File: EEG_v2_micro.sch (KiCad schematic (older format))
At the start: 34 parts, among them SW2 SW_PUSH, SW3 SW_PUSH, U6 CC2540, U7 2450BM15A0002E, X1 32-MHz, X2 32-MHz

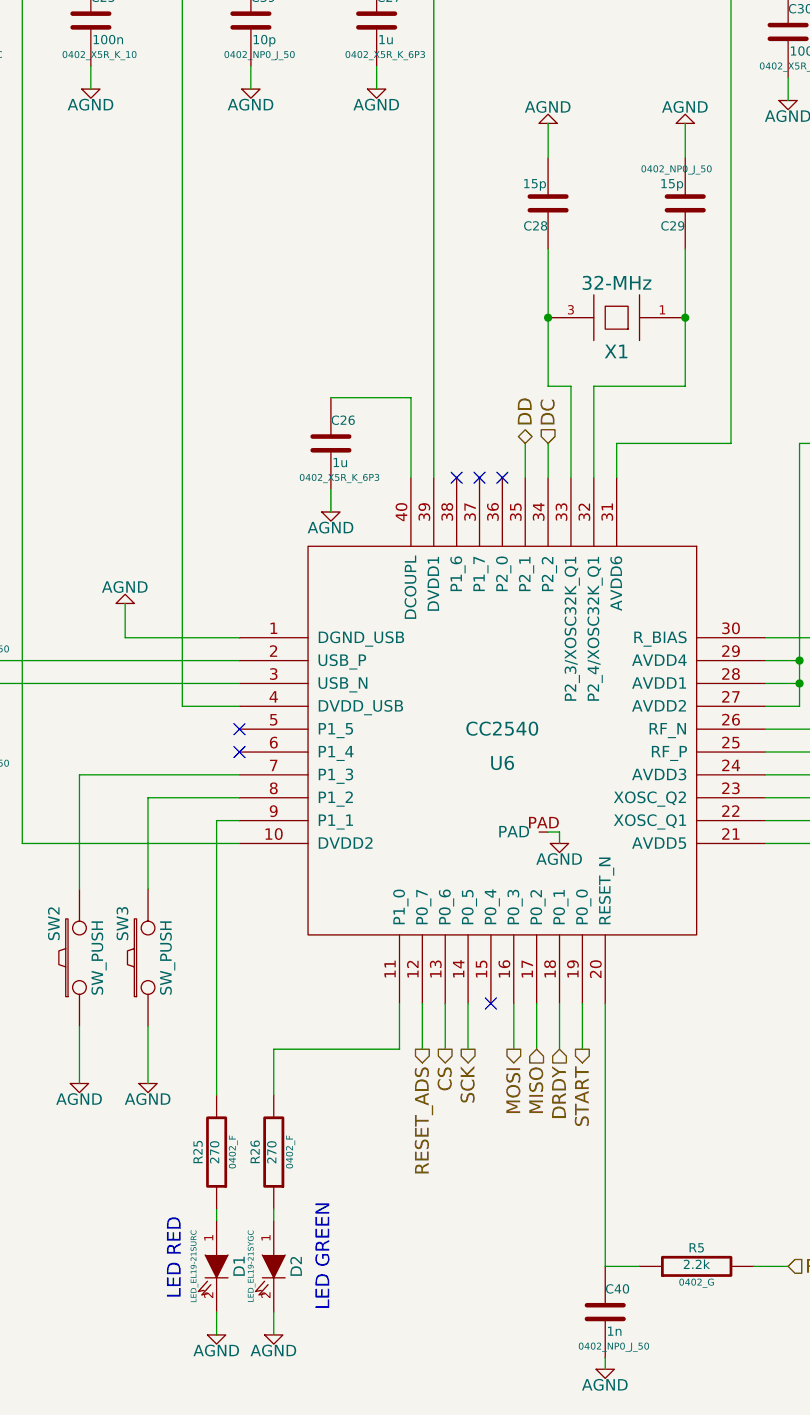
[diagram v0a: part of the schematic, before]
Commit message: Add footprints
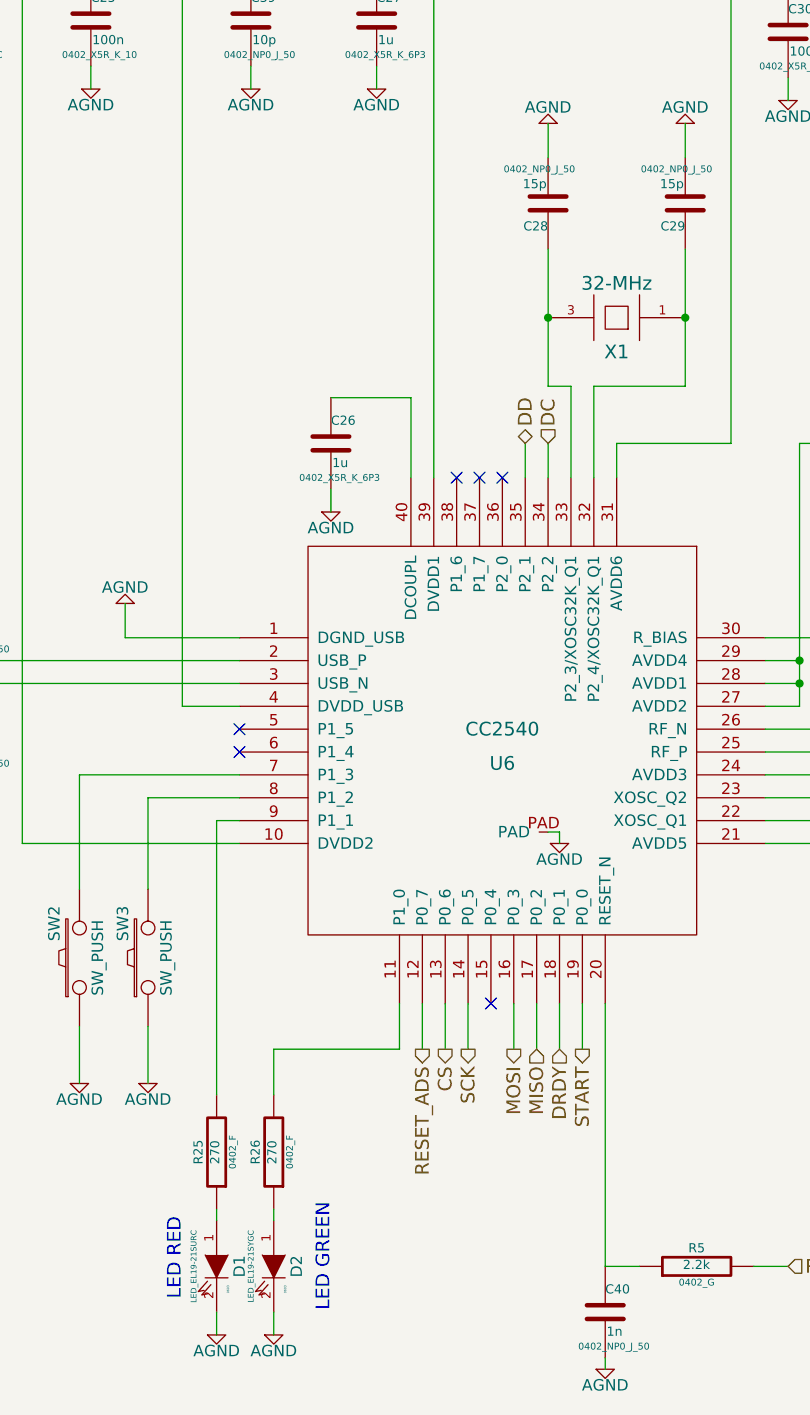
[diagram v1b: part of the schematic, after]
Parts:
- C28: footprint ~ -> 0402_NP0_J_50
- D1, D2: footprint ~ -> 0603
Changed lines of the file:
@@
 $EndComp
 $Comp
-L AGND #PWR038
+L AGND #PWR040
 U 1 1 54B4DC2F
 P 3400 3850
-F 0 "#PWR038" H 3400 3850 40  0001 C CNN
+F 0 "#PWR040" H 3400 3850 40  0001 C CNN
 F 1 "AGND" H 3400 3780 50  0000 C CNN
 F 2 "~" H 3400 3850 60  0000 C CNN
@@
 $EndComp
 $Comp
-L AGND #PWR039
+L AGND #PWR041
 U 1 1 54B4DEBC
 P 6550 4450
-F 0 "#PWR039" H 6550 4450 40  0001 C CNN
+F 0 "#PWR041" H 6550 4450 40  0001 C CNN
 F 1 "AGND" H 6550 4380 50  0000 C CNN
 F 2 "~" H 6550 4450 60  0000 C CNN
@@
 $EndComp
 $Comp
-L +3.3V #PWR040
+L +3.3V #PWR042
 U 1 1 54B4DF64
 P 650 1400
-F 0 "#PWR040" H 650 1360 30  0001 C CNN
+F 0 "#PWR042" H 650 1360 30  0001 C CNN
 F 1 "+3.3V" H 650 1510 30  0000 C CNN
 F 2 "~" H 650 1400 60  0000 C CNN
@@
 $EndComp
 $Comp
-L AGND #PWR041
+L AGND #PWR043
 U 1 1 54B4E155
 P 5750 6600
-F 0 "#PWR041" H 5750 6600 40  0001 C CNN
+F 0 "#PWR043" H 5750 6600 40  0001 C CNN
 F 1 "AGND" H 5750 6530 50  0000 C CNN
 F 2 "~" H 5750 6600 60  0000 C CNN
@@
 $EndComp
 $Comp
-L AGND #PWR042
+L AGND #PWR044
 U 1 1 54B4E15B
 P 6350 6600
-F 0 "#PWR042" H 6350 6600 40  0001 C CNN
+F 0 "#PWR044" H 6350 6600 40  0001 C CNN
 F 1 "AGND" H 6350 6530 50  0000 C CNN
 F 2 "~" H 6350 6600 60  0000 C CNN
@@
 F 0 "C28" H 4350 2600 40  0000 L CNN
 F 1 "15p" H 4356 2415 40  0000 L CNN
-F 2 "~" H 4388 2350 30  0000 C CNN
+F 2 "0402_NP0_J_50" H 4388 2350 30  0000 C CNN
 F 3 "~" H 4350 2500 60  0000 C CNN
 	1    4350 2500
@@
 $EndComp
 $Comp
-L AGND #PWR043
+L AGND #PWR045
 U 1 1 54B4E36D
 P 4950 2150
-F 0 "#PWR043" H 4950 2150 40  0001 C CNN
+F 0 "#PWR045" H 4950 2150 40  0001 C CNN
 F 1 "AGND" H 4950 2080 50  0000 C CNN
 F 2 "~" H 4950 2150 60  0000 C CNN
@@
 $EndComp
 $Comp
-L AGND #PWR044
+L AGND #PWR046
 U 1 1 54B4E373
 P 4350 2150
-F 0 "#PWR044" H 4350 2150 40  0001 C CNN
+F 0 "#PWR046" H 4350 2150 40  0001 C CNN
 F 1 "AGND" H 4350 2080 50  0000 C CNN
 F 2 "~" H 4350 2150 60  0000 C CNN
@@
 $EndComp
 $Comp
-L AGND #PWR045
+L AGND #PWR047
 U 1 1 54B4E516
 P 4400 5300
-F 0 "#PWR045" H 4400 5300 40  0001 C CNN
+F 0 "#PWR047" H 4400 5300 40  0001 C CNN
 F 1 "AGND" H 4400 5230 50  0000 C CNN
 F 2 "~" H 4400 5300 60  0000 C CNN
@@
 $EndComp
 $Comp
-L AGND #PWR046
+L AGND #PWR048
 U 1 1 54B4E69D
 P 2500 4250
-F 0 "#PWR046" H 2500 4250 40  0001 C CNN
+F 0 "#PWR048" H 2500 4250 40  0001 C CNN
 F 1 "AGND" H 2500 4180 50  0000 C CNN
 F 2 "~" H 2500 4250 60  0000 C CNN
@@
 $EndComp
 $Comp
-L AGND #PWR047
+L AGND #PWR049
 U 1 1 54B6FF14
 P 2350 2000
-F 0 "#PWR047" H 2350 2000 40  0001 C CNN
+F 0 "#PWR049" H 2350 2000 40  0001 C CNN
 F 1 "AGND" H 2350 1930 50  0000 C CNN
 F 2 "~" H 2350 2000 60  0000 C CNN
@@
 $EndComp
 $Comp
-L AGND #PWR048
+L AGND #PWR050
 U 1 1 54B7020B
 P 1700 2000
-F 0 "#PWR048" H 1700 2000 40  0001 C CNN
+F 0 "#PWR050" H 1700 2000 40  0001 C CNN
 F 1 "AGND" H 1700 1930 50  0000 C CNN
 F 2 "~" H 1700 2000 60  0000 C CNN
@@
 $EndComp
 $Comp
-L AGND #PWR049
+L AGND #PWR051
 U 1 1 54B703A3
 P 3600 2000
-F 0 "#PWR049" H 3600 2000 40  0001 C CNN
+F 0 "#PWR051" H 3600 2000 40  0001 C CNN
 F 1 "AGND" H 3600 1930 50  0000 C CNN
 F 2 "~" H 3600 2000 60  0000 C CNN
@@
 $EndComp
 $Comp
-L AGND #PWR050
+L AGND #PWR052
 U 1 1 54B708CD
 P 5400 2050
-F 0 "#PWR050" H 5400 2050 40  0001 C CNN
+F 0 "#PWR052" H 5400 2050 40  0001 C CNN
 F 1 "AGND" H 5400 1980 50  0000 C CNN
 F 2 "~" H 5400 2050 60  0000 C CNN
@@
 $EndComp
 $Comp
-L AGND #PWR051
+L AGND #PWR053
 U 1 1 54B70B07
 P 5950 2050
-F 0 "#PWR051" H 5950 2050 40  0001 C CNN
+F 0 "#PWR053" H 5950 2050 40  0001 C CNN
 F 1 "AGND" H 5950 1980 50  0000 C CNN
 F 2 "~" H 5950 2050 60  0000 C CNN
@@
 $EndComp
 $Comp
-L AGND #PWR052
+L AGND #PWR054
 U 1 1 54B70B14
 P 6350 2050
-F 0 "#PWR052" H 6350 2050 40  0001 C CNN
+F 0 "#PWR054" H 6350 2050 40  0001 C CNN
 F 1 "AGND" H 6350 1980 50  0000 C CNN
 F 2 "~" H 6350 2050 60  0000 C CNN
@@
 $EndComp
 $Comp
-L AGND #PWR053
+L AGND #PWR055
 U 1 1 54B71005
 P 6950 2050
-F 0 "#PWR053" H 6950 2050 40  0001 C CNN
+F 0 "#PWR055" H 6950 2050 40  0001 C CNN
 F 1 "AGND" H 6950 1980 50  0000 C CNN
 F 2 "~" H 6950 2050 60  0000 C CNN
@@
 $EndComp
 $Comp
-L AGND #PWR054
+L AGND #PWR056
 U 1 1 54B71061
 P 7500 2050
-F 0 "#PWR054" H 7500 2050 40  0001 C CNN
+F 0 "#PWR056" H 7500 2050 40  0001 C CNN
 F 1 "AGND" H 7500 1980 50  0000 C CNN
 F 2 "~" H 7500 2050 60  0000 C CNN
@@
 $EndComp
 $Comp
-L AGND #PWR055
+L AGND #PWR057
 U 1 1 54B71D5A
 P 8450 5400
-F 0 "#PWR055" H 8450 5400 40  0001 C CNN
+F 0 "#PWR057" H 8450 5400 40  0001 C CNN
 F 1 "AGND" H 8450 5330 50  0000 C CNN
 F 2 "~" H 8450 5400 60  0000 C CNN
@@
 $EndComp
 $Comp
-L AGND #PWR056
+L AGND #PWR058
 U 1 1 54B75306
 P 3050 2000
-F 0 "#PWR056" H 3050 2000 40  0001 C CNN
+F 0 "#PWR058" H 3050 2000 40  0001 C CNN
 F 1 "AGND" H 3050 1930 50  0000 C CNN
 F 2 "~" H 3050 2000 60  0000 C CNN
@@
 $EndComp
 $Comp
-L AGND #PWR057
+L AGND #PWR059
 U 1 1 54B75999
 P 1800 5050
-F 0 "#PWR057" H 1800 5050 40  0001 C CNN
+F 0 "#PWR059" H 1800 5050 40  0001 C CNN
 F 1 "AGND" H 1800 4980 50  0000 C CNN
 F 2 "~" H 1800 5050 60  0000 C CNN
@@
 $EndComp
 $Comp
-L AGND #PWR058
+L AGND #PWR060
 U 1 1 54B7599F
 P 1800 4000
-F 0 "#PWR058" H 1800 4000 40  0001 C CNN
+F 0 "#PWR060" H 1800 4000 40  0001 C CNN
 F 1 "AGND" H 1800 3930 50  0000 C CNN
 F 2 "~" H 1800 4000 60  0000 C CNN
@@
 	4600 6000 4600 7150
 $Comp
-L AGND #PWR059
+L AGND #PWR061
 U 1 1 54C2E9F6
 P 4600 7600
-F 0 "#PWR059" H 4600 7600 40  0001 C CNN
+F 0 "#PWR061" H 4600 7600 40  0001 C CNN
 F 1 "AGND" H 4600 7530 50  0000 C CNN
 F 2 "~" H 4600 7600 60  0000 C CNN
@@
 $EndComp
 $Comp
-L AGND #PWR060
+L AGND #PWR062
 U 1 1 54C2ED03
 P 9900 5550
-F 0 "#PWR060" H 9900 5550 40  0001 C CNN
+F 0 "#PWR062" H 9900 5550 40  0001 C CNN
 F 1 "AGND" H 9900 5480 50  0000 C CNN
 F 2 "~" H 9900 5550 60  0000 C CNN
@@
 $EndComp
 $Comp
-L AGND #PWR061
+L AGND #PWR063
 U 1 1 54C2EF06
 P 9450 4200
-F 0 "#PWR061" H 9450 4200 40  0001 C CNN
+F 0 "#PWR063" H 9450 4200 40  0001 C CNN
 F 1 "AGND" H 9450 4130 50  0000 C CNN
 F 2 "~" H 9450 4200 60  0000 C CNN
@@
 	2300 6100 2300 6350
 $Comp
-L AGND #PWR062
+L AGND #PWR064
 U 1 1 54CBF6E0
 P 2300 6350
-F 0 "#PWR062" H 2300 6350 40  0001 C CNN
+F 0 "#PWR064" H 2300 6350 40  0001 C CNN
 F 1 "AGND" H 2300 6280 50  0000 C CNN
 F 2 "~" H 2300 6350 60  0000 C CNN
@@
 	2600 6100 2600 6350
 $Comp
-L AGND #PWR063
+L AGND #PWR065
 U 1 1 54CBFC8B
 P 2600 6350
-F 0 "#PWR063" H 2600 6350 40  0001 C CNN
+F 0 "#PWR065" H 2600 6350 40  0001 C CNN
 F 1 "AGND" H 2600 6280 50  0000 C CNN
 F 2 "~" H 2600 6350 60  0000 C CNN
@@
 F 0 "D1" H 2900 7250 50  0000 C CNN
 F 1 "LED_EL19-21SURC" H 2900 7050 25  0000 C CNN
-F 2 "~" H 2900 7150 60  0000 C CNN
+F 2 "0603" H 3000 7200 10  0000 C CNN
 F 3 "~" H 2900 7150 60  0000 C CNN
 	1    2900 7150
@@
 F 0 "D2" H 3150 7250 50  0000 C CNN
 F 1 "LED_EL19-21SYGC" H 3150 7050 25  0000 C CNN
-F 2 "~" H 3150 7150 60  0000 C CNN
+F 2 "0603" H 3250 7200 10  0000 C CNN
 F 3 "~" H 3150 7150 60  0000 C CNN
 	1    3150 7150
@@
 	2900 6950 2900 6900
 $Comp
-L AGND #PWR064
+L AGND #PWR066
 U 1 1 54CC0292
 P 3150 7450
-F 0 "#PWR064" H 3150 7450 40  0001 C CNN
+F 0 "#PWR066" H 3150 7450 40  0001 C CNN
 F 1 "AGND" H 3150 7380 50  0000 C CNN
 F 2 "~" H 3150 7450 60  0000 C CNN
@@
 $EndComp
 $Comp
-L AGND #PWR065
+L AGND #PWR067
 U 1 1 54CC0298
 P 2900 7450
-F 0 "#PWR065" H 2900 7450 40  0001 C CNN
+F 0 "#PWR067" H 2900 7450 40  0001 C CNN
 F 1 "AGND" H 2900 7380 50  0000 C CNN
 F 2 "~" H 2900 7450 60  0000 C CNN
